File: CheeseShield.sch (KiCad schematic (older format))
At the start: 27 parts, among them J1 MS3 Toggle, J2 MS2 Toggle, J3 MS1 Toggle, J4 Power Screw Terminal, J5 JST XH_Stepper, J6 Temp2 3PinFan, J7 TempBed 3PinFan, J8 Temp1 3PinFan, J9 SSR Connection, M1 LM2596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

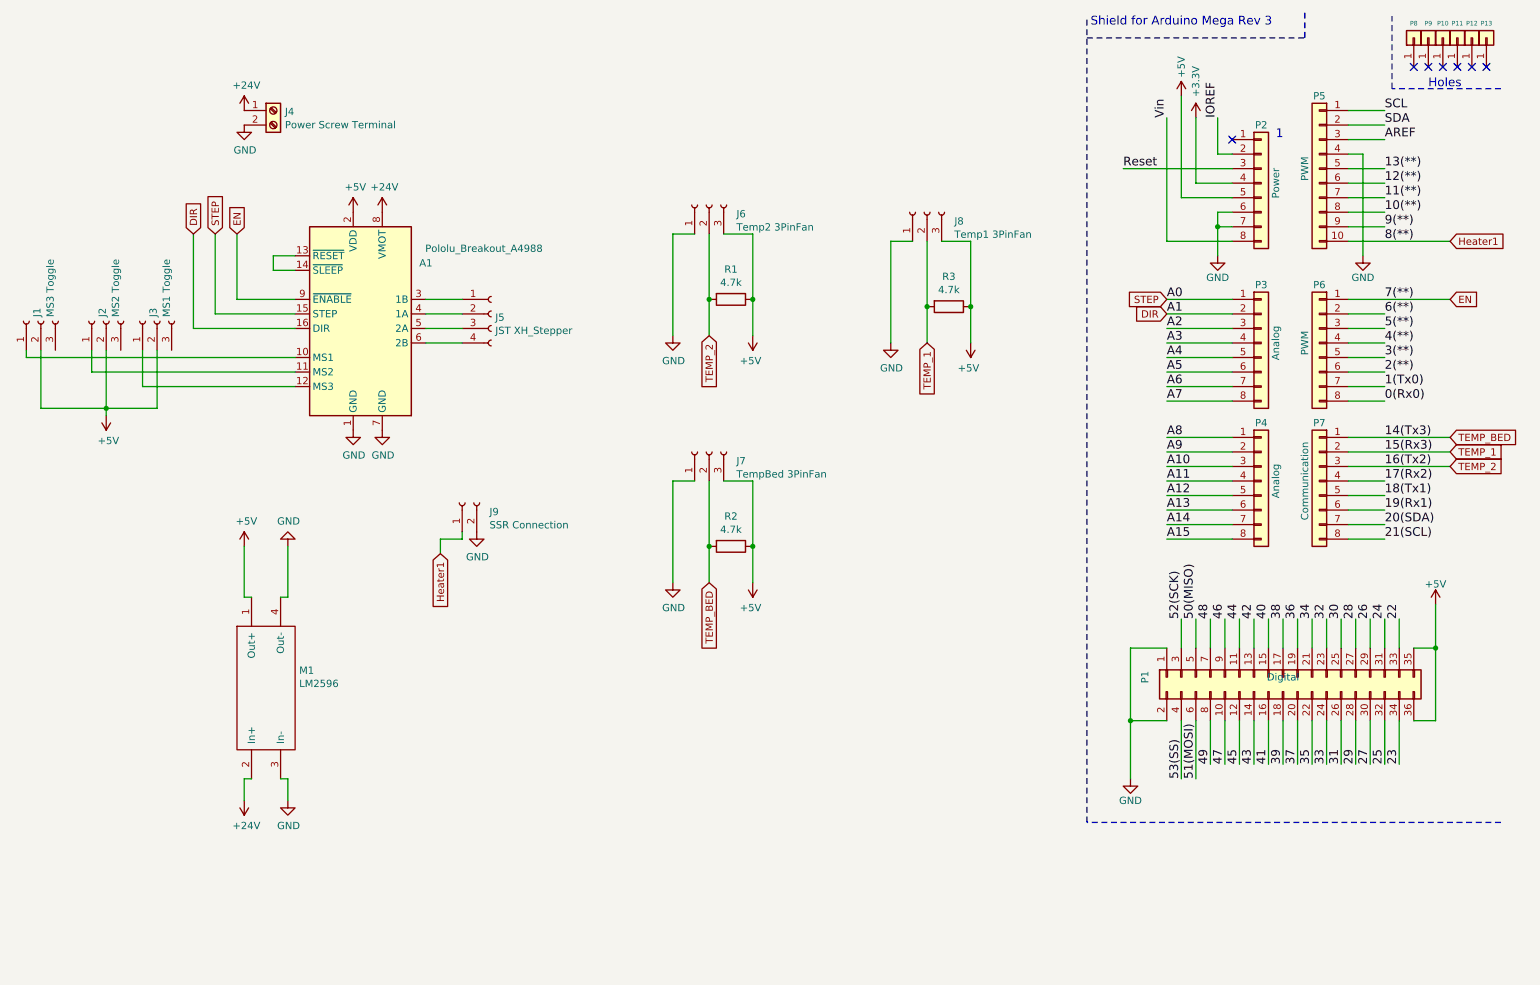
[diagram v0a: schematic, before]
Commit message: feat: Added in bluetooth and servo headers
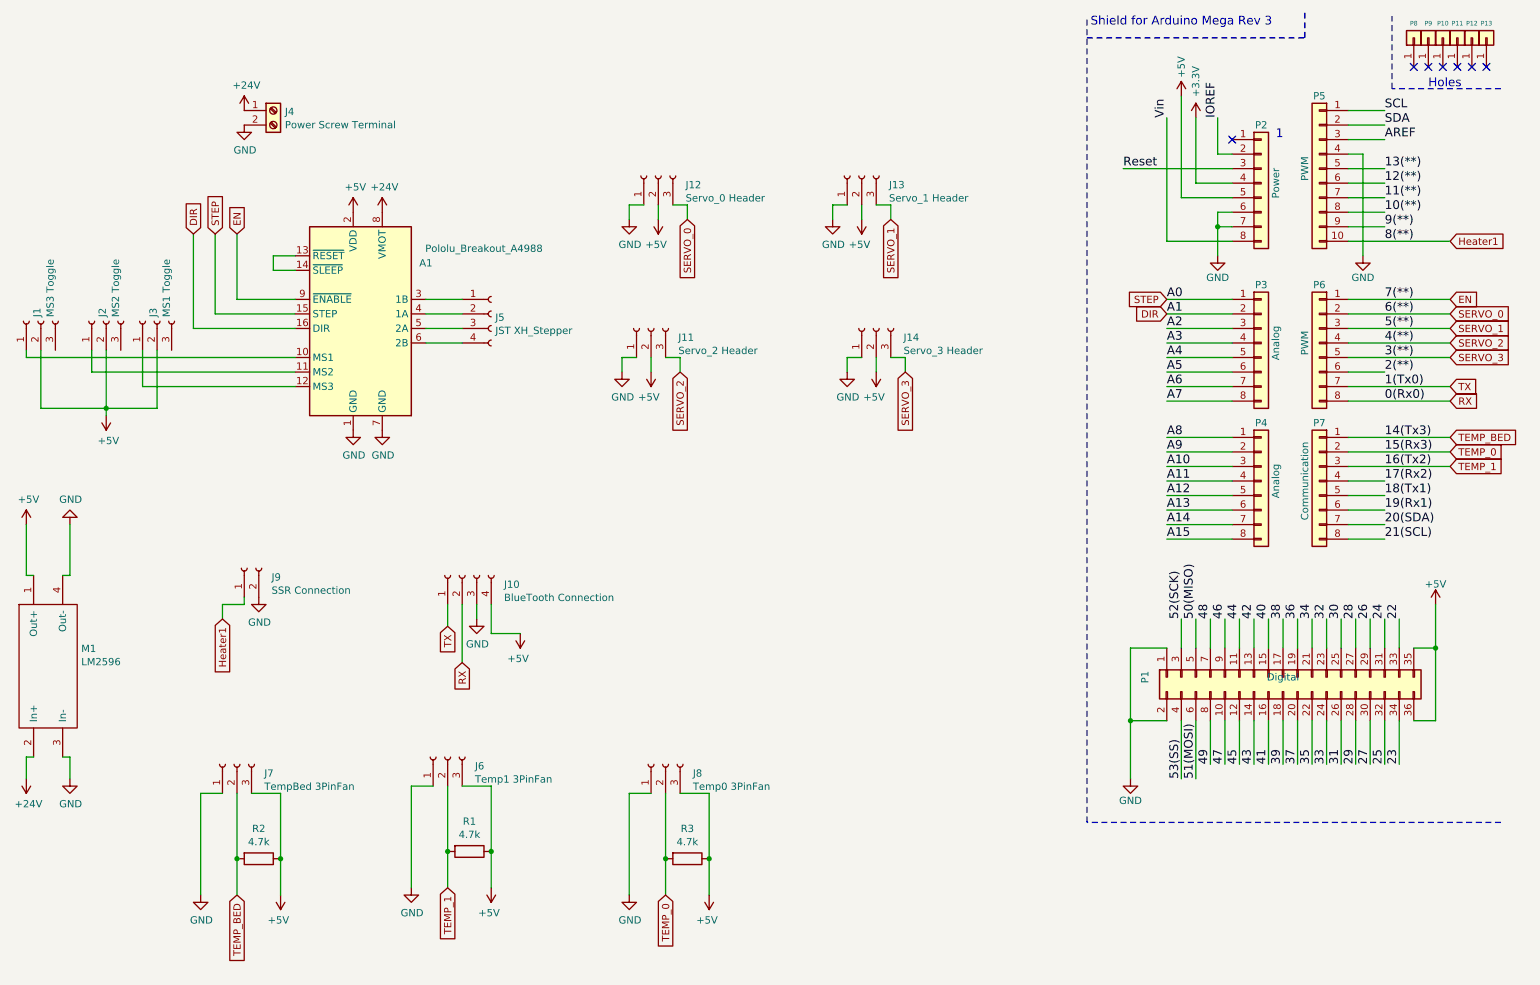
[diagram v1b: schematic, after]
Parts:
- added J10: BlueTooth Connection, Pin_Headers:Pin_Header_Straight_1x04_Pitch2.54mm, symbol Connector:Conn_01x04_Female
- added J11: Servo_2 Header, Pin_Headers:Pin_Header_Straight_1x03_Pitch2.54mm, symbol Connector:Conn_01x03_Female
- added J12: Servo_0 Header, Pin_Headers:Pin_Header_Straight_1x03_Pitch2.54mm, symbol Connector:Conn_01x03_Female
- added J13: Servo_1 Header, Pin_Headers:Pin_Header_Straight_1x03_Pitch2.54mm, symbol Connector:Conn_01x03_Female
- added J14: Servo_3 Header, Pin_Headers:Pin_Header_Straight_1x03_Pitch2.54mm, symbol Connector:Conn_01x03_Female
- J6: value Temp2 3PinFan -> Temp1 3PinFan
- J8: value Temp1 3PinFan -> Temp0 3PinFan
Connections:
- net TEMP_2 is gone; now on net TEMP_1: J6.2 (Pin_2), P7.3 (Pin_3), R1.2
- net +5V: now also J10.4 (Pin_4), J11.2 (Pin_2), J12.2 (Pin_2), J13.2 (Pin_2), J14.2 (Pin_2)
- net GND: now also J10.3 (Pin_3), J11.1 (Pin_1), J12.1 (Pin_1), J13.1 (Pin_1), J14.1 (Pin_1)
- net TEMP_1: no longer J8.2 (Pin_2), P7.2 (Pin_2), R3.2
- net 0(Rx0) renamed RX
- net RX: now also J10.2 (Pin_2)
- net 1(Tx0) renamed TX
- net TX: now also J10.1 (Pin_1)
- net 3(**) renamed SERVO_3
- net SERVO_3: now also J14.3 (Pin_3)
- net 4(**) renamed SERVO_2
- net SERVO_2: now also J11.3 (Pin_3)
- net 5(**) renamed SERVO_1
- net SERVO_1: now also J13.3 (Pin_3)
- net 6(**) renamed SERVO_0
- net SERVO_0: now also J12.3 (Pin_3)
- new net TEMP_0: J8.2 (Pin_2), P7.2 (Pin_2), R3.2
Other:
- moved on the sheet: J6, J7, J8, J9, M1, R1, R2, R3
